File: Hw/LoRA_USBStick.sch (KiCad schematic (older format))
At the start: 21 parts, among them J10 USB_B, J4 SWD, J5 Serial, SW1 RST, U1 ATSAMD21E, U2 RFM95W-868S2, U7 AP2114H-3.3TRG1

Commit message: Update kicad 5
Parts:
- AE1: symbol Antenna_Shield -> Device:Antenna_Shield
- C3, C4, C5, C6, C7: symbol C -> Device:C
- D6, D7: symbol LED_Small -> Device:LED_Small
- J10: symbol USB_B -> LoRA_USBStick-rescue:USB_B
- J4: symbol Conn_01x04 -> LoRA_USBStick-rescue:Conn_01x04
- J5: symbol Conn_01x03 -> LoRA_USBStick-rescue:Conn_01x03
- MK1, MK2, MK3, MK4: symbol Mounting_Hole -> LoRA_USBStick-rescue:Mounting_Hole
- R11, R9: symbol R_Small -> Device:R_Small
- SW1: symbol SW_Push -> LoRA_USBStick-rescue:SW_Push
- U1: symbol ATSAMD21E -> agroin:ATSAMD21E
- U2: symbol RFM95W-868S2 -> agroin:RFM95W-868S2
- U7: symbol AP2114H-3.3TRG1 -> agroin:AP2114H-3.3TRG1
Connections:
- wire segments 51 -> 58

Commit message: Update measure for case
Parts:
- J10: footprint USB:629105150521 -> USB:629004113921
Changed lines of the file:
@@
 F 0 "J10" H 4705 5340 50  0000 L CNN
 F 1 "USB_B" H 4705 5240 50  0000 L CNN
-F 2 "USB:629105150521" H 5055 4840 50  0001 C CNN
+F 2 "USB:629004113921" H 5055 4840 50  0001 C CNN
 F 3 "" H 5055 4840 50  0001 C CNN
 	1    4905 4890

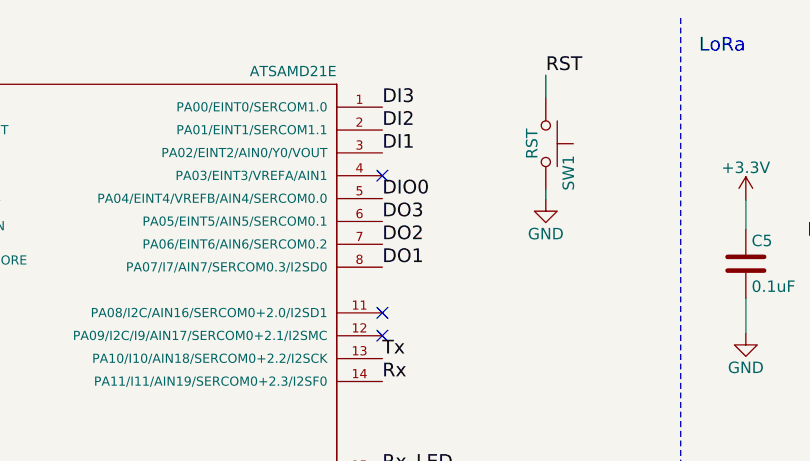
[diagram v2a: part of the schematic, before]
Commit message: Clean GPIO not use
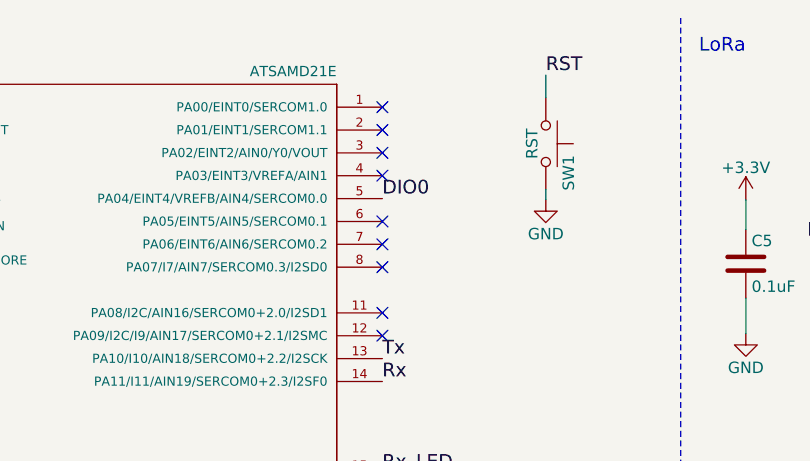
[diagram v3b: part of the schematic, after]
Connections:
- net labels removed: DI1, DI2, DI3, DO1, DO2, DO3
- no-connect marks 6 -> 12
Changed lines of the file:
@@
 Sheet 1 1
 Title "USB Stick"
-Date "2018-05-28"
-Rev "0.1"
+Date "2018-11-25"
+Rev "0.2"
 Comp "Electronic Cats"
 Comment1 "Eduardo Contreras"
-Comment2 ""
+Comment2 "Andres Sabas"
 Comment3 ""
 Comment4 ""
@@
 Text Label 9200 2050 2    60   ~ 0
 DIO2
-Text Label 9200 1550 2    60   ~ 0
-DIO5
 Text Notes 4360 600  0    60   ~ 0
 Microcontroller
@@
 Wire Wire Line
 	7680 725  7680 825
-Text Label 6965 1365 0    60   ~ 0
-DO3
-Text Label 6965 1465 0    60   ~ 0
-DO2
-Text Label 6965 1565 0    60   ~ 0
-DO1
-Text Label 6965 865  0    60   ~ 0
-DI3
-Text Label 6965 965  0    60   ~ 0
-DI2
-Text Label 6965 1065 0    60   ~ 0
-DI1
 Text Label 7340 4755 2    60   ~ 0
 Tx
@@
 Wire Notes Line
 	2290 2365 2290 6540
+NoConn ~ 6965 1565
+NoConn ~ 6965 1465
+NoConn ~ 6965 1365
+NoConn ~ 6965 865
+NoConn ~ 6965 965
+NoConn ~ 6965 1065
+Text Label 9200 1550 2    60   ~ 0
+DIO5
 $EndSCHEMATC

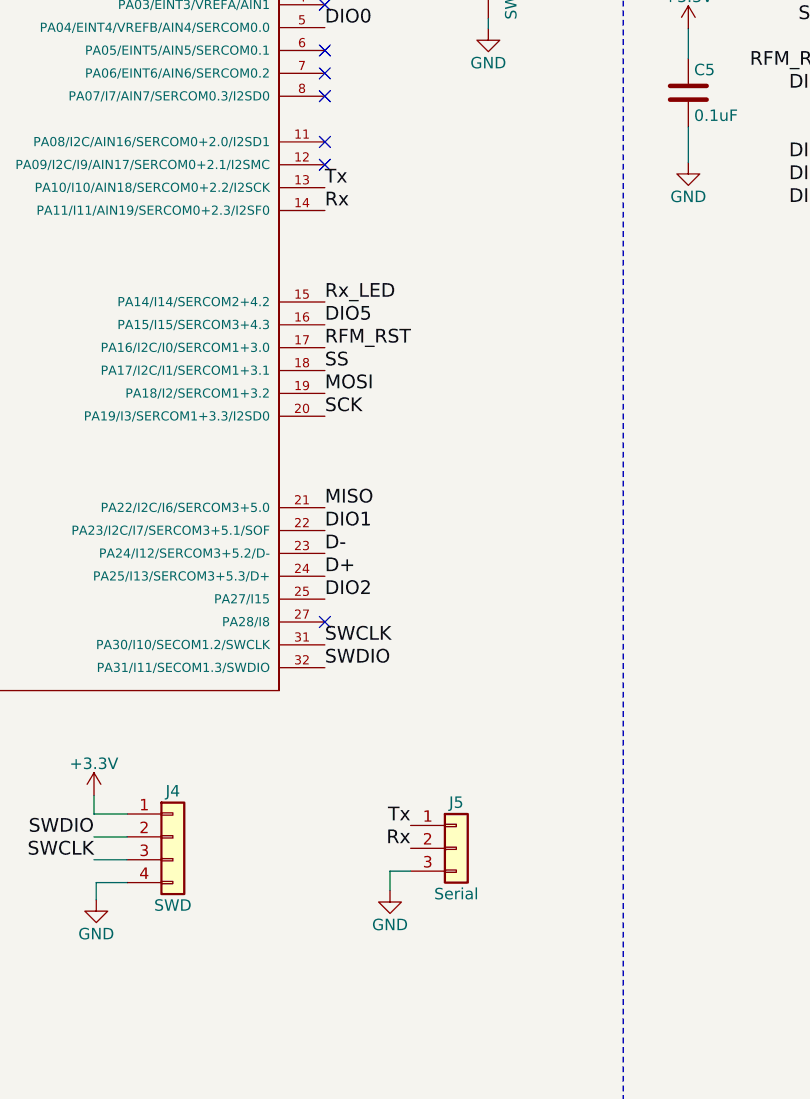
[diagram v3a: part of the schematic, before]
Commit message: Remove TX and RX not used
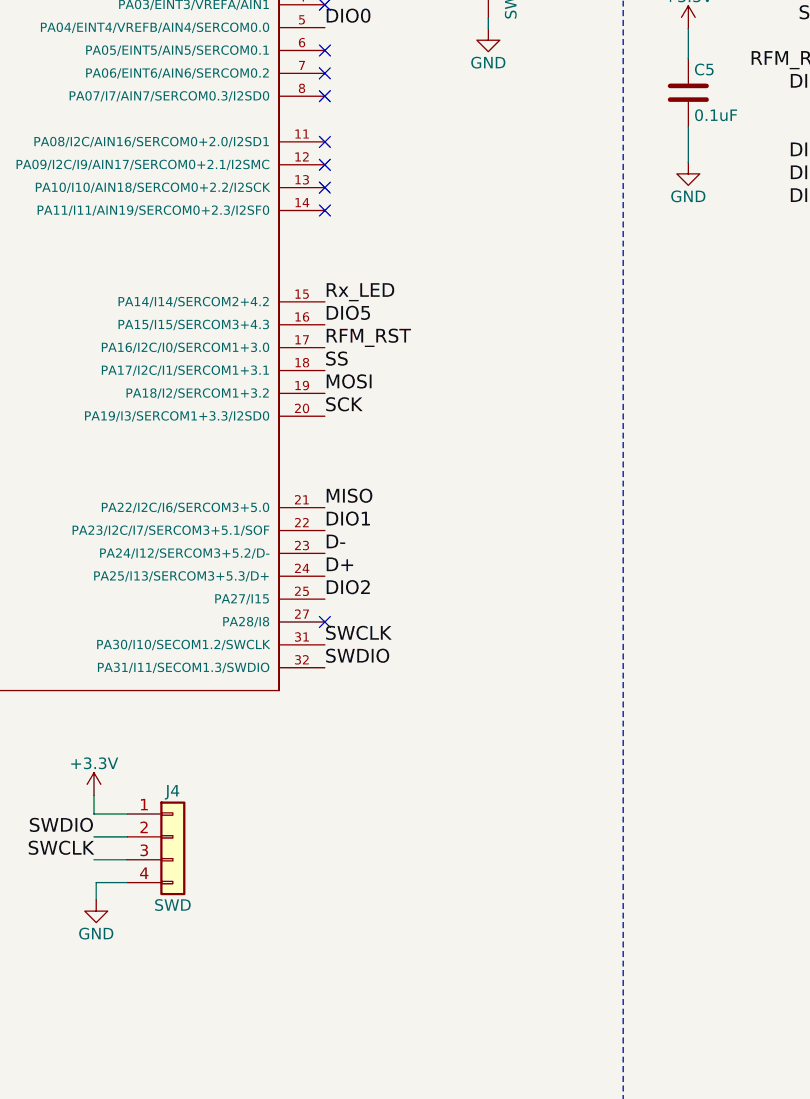
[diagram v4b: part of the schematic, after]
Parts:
- removed J5: Serial, Pin_Headers:Pin_Header_Straight_1x03_Pitch2.54mm, symbol LoRA_USBStick-rescue:Conn_01x03
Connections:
- net labels removed: Rx, Tx
- wire segments 58 -> 56
- no-connect marks 12 -> 14
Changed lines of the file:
@@
 Text Label 6965 3765 0    60   ~ 0
 DIO2
-Text Label 6965 2065 0    60   ~ 0
-Rx
-Text Label 6965 1965 0    60   ~ 0
-Tx
 $Comp
 L agroin:ATSAMD21E U1
@@
 $EndComp
 $Comp
-L power:GND #PWR011
-U 1 1 5B050555
-P 7250 5040
-F 0 "#PWR011" H 7250 4790 50  0001 C CNN
-F 1 "GND" H 7250 4890 50  0000 C CNN
-F 2 "" H 7250 5040 50  0001 C CNN
-F 3 "" H 7250 5040 50  0001 C CNN
-	1    7250 5040
-	1    0    0    -1
-$EndComp
-$Comp
 L power:+3.3V #PWR012
 U 1 1 5B050850
@@
 Wire Wire Line
 	5965 5005 6100 5005
-$Comp
-L LoRA_USBStick-rescue:Conn_01x03 J5
-U 1 1 5B066480
-P 7540 4855
-F 0 "J5" H 7540 5055 50  0000 C CNN
-F 1 "Serial" H 7540 4655 50  0000 C CNN
-F 2 "Pin_Headers:Pin_Header_Straight_1x03_Pitch2.54mm" H 7540 4855 50  0001 C CNN
-F 3 "" H 7540 4855 50  0001 C CNN
-	1    7540 4855
-	1    0    0    -1
-$EndComp
 Wire Wire Line
 	7680 725  7680 825
-Text Label 7340 4755 2    60   ~ 0
-Tx
-Text Label 7340 4855 2    60   ~ 0
-Rx
-Wire Wire Line
-	7250 5040 7250 4955
-Wire Wire Line
-	7250 4955 7340 4955
 $Comp
 L Device:Antenna_Shield AE1
@@
 Text Label 9200 1550 2    60   ~ 0
 DIO5
+NoConn ~ 6965 1965
+NoConn ~ 6965 2065
 $EndSCHEMATC

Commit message: Update V3.0
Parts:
- SW1: footprint Buttons_Switches_SMD:SW_SPST_B3U-1000P -> Button_Switch_SMD:SW_SPST_TL3342
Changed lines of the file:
@@
 F 0 "SW1" H 7730 1125 50  0000 L CNN
 F 1 "RST" H 7680 965 50  0000 C CNN
-F 2 "Buttons_Switches_SMD:SW_SPST_B3U-1000P" H 7680 1225 50  0001 C CNN
+F 2 "Button_Switch_SMD:SW_SPST_TL3342" H 7680 1225 50  0001 C CNN
 F 3 "" H 7680 1225 50  0001 C CNN
 F 4 "B3U-1000P" H 7680 1025 60  0001 C CNN "manf#"

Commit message: Update board 2.4v
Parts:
- removed MK1, MK2, MK3, MK4: Mounting_Hole, Mounting_Holes:MountingHole_3.5mm_Pad_Via, symbol LoRA_USBStick-rescue:Mounting_Hole
- removed U7: AP2114H-3.3TRG1, TO_SOT_Packages_SMD:SOT-223-3Lead_TabPin2, symbol agroin:AP2114H-3.3TRG1
- added U3: AP2112K-3.3, Package_TO_SOT_SMD:SOT-23-5, symbol Regulator_Linear:AP2112K-3.3
- C3, C4, C5, C6, C7: footprint Capacitors_SMD:C_0805_HandSoldering -> Capacitor_SMD:C_0805_2012Metric_Pad1.15x1.40mm_HandSolder
- D1: renamed from D7; footprint LEDs:LED_0805_HandSoldering -> LED_SMD:LED_0805_2012Metric_Pad1.15x1.40mm_HandSolder
- D2: renamed from D6; footprint LEDs:LED_0805_HandSoldering -> LED_SMD:LED_0805_2012Metric_Pad1.15x1.40mm_HandSolder
- J10: footprint USB:629004113921 -> Connectors:C46394
- R11, R9: footprint Resistors_SMD:R_0805_HandSoldering -> Resistor_SMD:R_0805_2012Metric_Pad1.15x1.40mm_HandSolder
- U2: footprint agroin:RFM95W -> RF_Module:HOPERF_RFM9XW_SMD; Field4 RFM95W-868S2 -> (none); Field5 Warning -> (none); Field6 7.22 USD -> (none); Field7 RF -> (none)
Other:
- note removed: "Mounting holes"
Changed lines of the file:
@@
 EESchema Schematic File Version 4
 LIBS:LoRA_USBStick-cache
-EELAYER 26 0
+EELAYER 29 0
 EELAYER END
 $Descr A4 11693 8268
@@
 Sheet 1 1
 Title "USB Stick"
-Date "2018-11-25"
-Rev "0.2"
+Date "2020-01-09"
+Rev "1.1"
 Comp "Electronic Cats"
 Comment1 "Eduardo Contreras"
@@
 F 0 "C4" H 4845 2980 50  0000 L CNN
 F 1 "0.1uF" H 4845 2780 50  0000 L CNN
-F 2 "Capacitors_SMD:C_0805_HandSoldering" H 4858 2730 50  0001 C CNN
+F 2 "Capacitor_SMD:C_0805_2012Metric_Pad1.15x1.40mm_HandSolder" H 4858 2730 50  0001 C CNN
 F 3 "" H 4820 2880 50  0001 C CNN
 F 4 "885012207072" H 4820 2880 60  0001 C CNN "manf#"
@@
 F 0 "C5" H 8580 1650 50  0000 L CNN
 F 1 "0.1uF" H 8580 1450 50  0000 L CNN
-F 2 "Capacitors_SMD:C_0805_HandSoldering" H 8593 1400 50  0001 C CNN
+F 2 "Capacitor_SMD:C_0805_2012Metric_Pad1.15x1.40mm_HandSolder" H 8593 1400 50  0001 C CNN
 F 3 "" H 8555 1550 50  0001 C CNN
 F 4 "885012207072" H 8555 1550 60  0001 C CNN "manf#"
@@
 F 0 "U2" H 9299 2101 50  0000 L BNN
 F 1 "RFM95W-868S2" H 9298 848 50  0000 L BNN
-F 2 "agroin:RFM95W" H 9900 1550 50  0001 L BNN
-F 3 "SMD-16 Hope Microelectronics" H 9650 1400 50  0001 L BNN
-F 4 "RFM95W-868S2" H 9900 1550 50  0001 L BNN "Field4"
-F 5 "Warning" H 9900 1550 50  0001 L BNN "Field5"
-F 6 "7.22 USD" H 9900 1550 50  0001 L BNN "Field6"
-F 7 "RF" H 9900 1550 50  0001 L BNN "Field7"
+F 2 "RF_Module:HOPERF_RFM9XW_SMD" H 9900 1550 50  0001 L BNN
+F 3 "" H 9650 1400 50  0001 L BNN
 	1    9900 1550
 	1    0    0    -1
@@
 F 0 "C3" H 4845 1910 50  0000 L CNN
 F 1 "1uF" H 4845 1710 50  0000 L CNN
-F 2 "Capacitors_SMD:C_0805_HandSoldering" H 4858 1660 50  0001 C CNN
+F 2 "Capacitor_SMD:C_0805_2012Metric_Pad1.15x1.40mm_HandSolder" H 4858 1660 50  0001 C CNN
 F 3 "" H 4820 1810 50  0001 C CNN
 F 4 "GRM21BC80J106KE19L" H 4820 1810 60  0001 C CNN "manf#"
@@
 	11220 4565 11220 4560
 $Comp
-L LoRA_USBStick-rescue:Mounting_Hole MK1
-U 1 1 5B0810C4
-P 4730 7195
-F 0 "MK1" H 4730 7395 50  0000 C CNN
-F 1 "Mounting_Hole" H 4730 7320 50  0000 C CNN
-F 2 "Mounting_Holes:MountingHole_3.5mm_Pad_Via" H 4730 7195 50  0001 C CNN
-F 3 "" H 4730 7195 50  0001 C CNN
-	1    4730 7195
-	1    0    0    -1
-$EndComp
-$Comp
-L LoRA_USBStick-rescue:Mounting_Hole MK3
-U 1 1 5B081269
-P 5315 7200
-F 0 "MK3" H 5315 7400 50  0000 C CNN
-F 1 "Mounting_Hole" H 5315 7325 50  0000 C CNN
-F 2 "Mounting_Holes:MountingHole_3.5mm_Pad_Via" H 5315 7200 50  0001 C CNN
-F 3 "" H 5315 7200 50  0001 C CNN
-	1    5315 7200
-	1    0    0    -1
-$EndComp
-$Comp
-L LoRA_USBStick-rescue:Mounting_Hole MK2
-U 1 1 5B081339
-P 5960 7195
-F 0 "MK2" H 5960 7395 50  0000 C CNN
-F 1 "Mounting_Hole" H 5960 7320 50  0000 C CNN
-F 2 "Mounting_Holes:MountingHole_3.5mm_Pad_Via" H 5960 7195 50  0001 C CNN
-F 3 "" H 5960 7195 50  0001 C CNN
-	1    5960 7195
-	1    0    0    -1
-$EndComp
-$Comp
-L LoRA_USBStick-rescue:Mounting_Hole MK4
-U 1 1 5B0813F3
-P 6595 7200
-F 0 "MK4" H 6595 7400 50  0000 C CNN
-F 1 "Mounting_Hole" H 6595 7325 50  0000 C CNN
-F 2 "Mounting_Holes:MountingHole_3.5mm_Pad_Via" H 6595 7200 50  0001 C CNN
-F 3 "" H 6595 7200 50  0001 C CNN
-	1    6595 7200
-	1    0    0    -1
-$EndComp
-Text Notes 4370 6665 0    60   ~ 0
-Mounting holes
-$Comp
 L power:GND #PWR014
 U 1 1 5B08A6AC
@@
 USB voltage regulator\n
 $Comp
-L agroin:AP2114H-3.3TRG1 U7
-U 1 1 5B0CCD1F
-P 1865 1380
-F 0 "U7" H 1655 1640 50  0000 C CNN
-F 1 "AP2114H-3.3TRG1" H 1545 1575 50  0000 L CNN
-F 2 "TO_SOT_Packages_SMD:SOT-223-3Lead_TabPin2" H 1405 1650 50  0001 C CIN
-F 3 "" H 1865 1380 50  0001 C CNN
-F 4 "AP2114H-3.3TRG1" H 1865 1380 60  0001 C CNN "manf#"
-	1    1865 1380
-	1    0    0    -1
-$EndComp
-$Comp
 L power:VBUS #PWR017
 U 1 1 5B0CD86E
@@
 $EndComp
 Wire Wire Line
-	1465 1330 1395 1330
-Wire Wire Line
 	1315 1330 1315 1265
-Wire Wire Line
-	2265 1330 2355 1330
 $Comp
 L power:GND #PWR018
 U 1 1 5B0CEDD6
-P 1865 1685
-F 0 "#PWR018" H 1865 1435 50  0001 C CNN
-F 1 "GND" H 1865 1535 50  0000 C CNN
-F 2 "" H 1865 1685 50  0001 C CNN
-F 3 "" H 1865 1685 50  0001 C CNN
-	1    1865 1685
-	1    0    0    -1
-$EndComp
-Wire Wire Line
-	1865 1630 1865 1685
+P 1865 1785
+F 0 "#PWR018" H 1865 1535 50  0001 C CNN
+F 1 "GND" H 1865 1635 50  0000 C CNN
+F 2 "" H 1865 1785 50  0001 C CNN
+F 3 "" H 1865 1785 50  0001 C CNN
+	1    1865 1785
+	1    0    0    -1
+$EndComp
 $Comp
 L Device:C C7
@@
 F 0 "C7" H 2380 1625 50  0000 L CNN
 F 1 "10uF" H 2380 1425 50  0000 L CNN
-F 2 "Capacitors_SMD:C_0805_HandSoldering" H 2393 1375 50  0001 C CNN
+F 2 "Capacitor_SMD:C_0805_2012Metric_Pad1.15x1.40mm_HandSolder" H 2393 1375 50  0001 C CNN
 F 3 "" H 2355 1525 50  0001 C CNN
 F 4 "GRM21BC80J106KE19L" H 2355 1525 60  0001 C CNN "manf#"
@@
 F 0 "C6" H 1420 1615 50  0000 L CNN
 F 1 "10uF" H 1420 1415 50  0000 L CNN
-F 2 "Capacitors_SMD:C_0805_HandSoldering" H 1433 1365 50  0001 C CNN
+F 2 "Capacitor_SMD:C_0805_2012Metric_Pad1.15x1.40mm_HandSolder" H 1433 1365 50  0001 C CNN
 F 3 "" H 1395 1515 50  0001 C CNN
 F 4 "GRM21BC80J106KE19L" H 1395 1515 60  0001 C CNN "manf#"
@@
 Led's indicators
 $Comp
-L Device:LED_Small D7
+L Device:LED_Small D1
 U 1 1 5B0D290D
 P 2930 3185
-F 0 "D7" H 2880 3310 50  0000 L CNN
+F 0 "D1" H 2880 3310 50  0000 L CNN
 F 1 "Rx" V 2930 3045 50  0000 L CNN
-F 2 "LEDs:LED_0805_HandSoldering" V 2930 3185 50  0001 C CNN
+F 2 "LED_SMD:LED_0805_2012Metric_Pad1.15x1.40mm_HandSolder" V 2930 3185 50  0001 C CNN
 F 3 "" V 2930 3185 50  0001 C CNN
 F 4 "APT2012SGC" H 2930 3185 60  0001 C CNN "manf#"
@@
 $EndComp
 $Comp
-L Device:LED_Small D6
+L Device:LED_Small D2
 U 1 1 5B0D2AA0
 P 3635 3175
-F 0 "D6" H 3585 3300 50  0000 L CNN
+F 0 "D2" H 3585 3300 50  0000 L CNN
 F 1 "ON" V 3635 3015 50  0000 L CNN
-F 2 "LEDs:LED_0805_HandSoldering" V 3635 3175 50  0001 C CNN
+F 2 "LED_SMD:LED_0805_2012Metric_Pad1.15x1.40mm_HandSolder" V 3635 3175 50  0001 C CNN
 F 3 "" V 3635 3175 50  0001 C CNN
 F 4 "AP2012EC" H 3635 3175 60  0001 C CNN "manf#"
@@
 F 0 "R9" H 3665 2910 50  0000 L CNN
 F 1 "120R" H 3665 2850 50  0000 L CNN
-F 2 "Resistors_SMD:R_0805_HandSoldering" H 3635 2890 50  0001 C CNN
+F 2 "Resistor_SMD:R_0805_2012Metric_Pad1.15x1.40mm_HandSolder" H 3635 2890 50  0001 C CNN
 F 3 "" H 3635 2890 50  0001 C CNN
 F 4 "RMC1/10K1200FTP" H 3635 2890 60  0001 C CNN "manf#"
@@
 F 0 "R11" H 2960 2935 50  0000 L CNN
 F 1 "120R" H 2960 2875 50  0000 L CNN
-F 2 "Resistors_SMD:R_0805_HandSoldering" H 2930 2915 50  0001 C CNN
+F 2 "Resistor_SMD:R_0805_2012Metric_Pad1.15x1.40mm_HandSolder" H 2930 2915 50  0001 C CNN
 F 3 "" H 2930 2915 50  0001 C CNN
 F 4 "RMC1/10K1200FTP" H 2930 2915 60  0001 C CNN "manf#"
@@
 F 0 "J10" H 4705 5340 50  0000 L CNN
 F 1 "USB_B" H 4705 5240 50  0000 L CNN
-F 2 "USB:629004113921" H 5055 4840 50  0001 C CNN
+F 2 "Connectors:C46394" H 5055 4840 50  0001 C CNN
 F 3 "" H 5055 4840 50  0001 C CNN
 	1    4905 4890
@@
 NoConn ~ 6965 1965
 NoConn ~ 6965 2065
+$Comp
+L Regulator_Linear:AP2112K-3.3 U3
+U 1 1 5E1F7A40
+P 1865 1430
+F 0 "U3" H 1865 1772 50  0000 C CNN
+F 1 "AP2112K-3.3" H 1865 1681 50  0000 C CNN
+F 2 "Package_TO_SOT_SMD:SOT-23-5" H 1865 1755 50  0001 C CNN
+F 3 "https://www.diodes.com/assets/Datasheets/AP2112.pdf" H 1865 1530 50  0001 C CNN
+	1    1865 1430
+	1    0    0    -1
+$EndComp
+Wire Wire Line
+	1395 1330 1565 1330
+Wire Wire Line
+	1865 1730 1865 1785
+Wire Wire Line
+	2165 1330 2355 1330
 $EndSCHEMATC

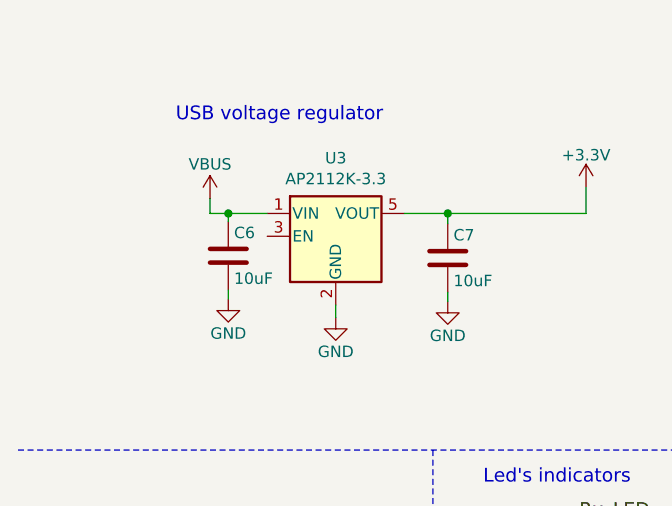
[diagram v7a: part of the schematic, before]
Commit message: fix enable LDO
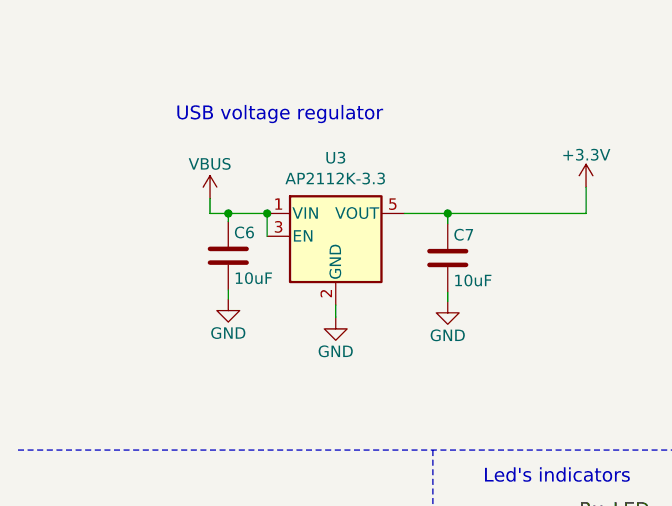
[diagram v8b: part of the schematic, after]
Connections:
- net VBUS: now also U3.3 (EN)
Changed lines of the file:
@@
 EESchema Schematic File Version 4
-LIBS:LoRA_USBStick-cache
-EELAYER 29 0
+EELAYER 30 0
 EELAYER END
 $Descr A4 11693 8268
@@
 Sheet 1 1
 Title "USB Stick"
-Date "2020-01-09"
-Rev "2.4"
+Date "2020-08-03"
+Rev "2.5"
 Comp "Electronic Cats"
 Comment1 "Eduardo Contreras"
@@
 $EndComp
 Wire Wire Line
+	1865 1730 1865 1785
+Wire Wire Line
+	2165 1330 2355 1330
+Wire Wire Line
 	1395 1330 1565 1330
 Wire Wire Line
-	1865 1730 1865 1785
-Wire Wire Line
-	2165 1330 2355 1330
+	1565 1430 1565 1330
+Connection ~ 1565 1330
 $EndSCHEMATC
